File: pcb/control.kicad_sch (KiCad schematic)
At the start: 3 parts, among them J11 Conn_01x02_Pin

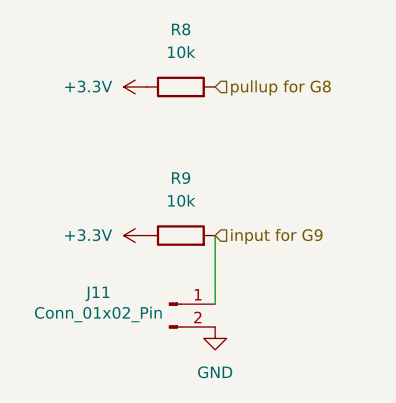
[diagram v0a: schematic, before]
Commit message: Finishing the carrier board with the new usb-c modul
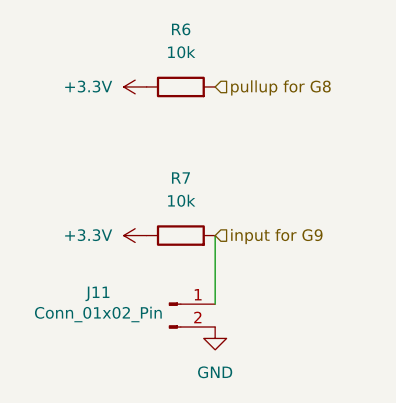
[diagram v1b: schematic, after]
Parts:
- renumbered R8 to R6, R9 to R7
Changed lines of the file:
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@@
 		(dnp no)
 		(fields_autoplaced yes)
-		(property "Reference" "#PWR033"
+		(property "Reference" "#PWR031"
 			(at 124.46 111.76 0)
 			(hide yes)
@@
 			(project "pcb"
 				(path "/2955ee96-3683-4cf6-bfa3-83b5e4980920/6ba59ddd-18a4-4e0c-ad10-73ba465496e1"
-					(reference "#PWR033")
+					(reference "#PWR031")
 					(unit 1)
 				)
@@
 		(dnp no)
 		(fields_autoplaced yes)
-		(property "Reference" "R8"
+		(property "Reference" "R6"
 			(at 120.65 72.39 90)
 			(show_name no)
@@
 			(project "pcb"
 				(path "/2955ee96-3683-4cf6-bfa3-83b5e4980920/6ba59ddd-18a4-4e0c-ad10-73ba465496e1"
-					(reference "R8")
+					(reference "R6")
 					(unit 1)
 				)
@@
 		(dnp no)
 		(fields_autoplaced yes)
-		(property "Reference" "#PWR032"
+		(property "Reference" "#PWR030"
 			(at 120.65 95.25 0)
 			(hide yes)
@@
 			(project "pcb"
 				(path "/2955ee96-3683-4cf6-bfa3-83b5e4980920/6ba59ddd-18a4-4e0c-ad10-73ba465496e1"
-					(reference "#PWR032")
+					(reference "#PWR030")
 					(unit 1)
 				)
@@
 		(dnp no)
 		(fields_autoplaced yes)
-		(property "Reference" "#PWR031"
+		(property "Reference" "#PWR029"
 			(at 120.65 78.74 0)
 			(hide yes)
@@
 			(project "pcb"
 				(path "/2955ee96-3683-4cf6-bfa3-83b5e4980920/6ba59ddd-18a4-4e0c-ad10-73ba465496e1"
-					(reference "#PWR031")
+					(reference "#PWR029")
 					(unit 1)
 				)
@@
 		(dnp no)
 		(fields_autoplaced yes)
-		(property "Reference" "R9"
+		(property "Reference" "R7"
 			(at 120.65 88.9 90)
 			(show_name no)
@@
 			(project "pcb"
 				(path "/2955ee96-3683-4cf6-bfa3-83b5e4980920/6ba59ddd-18a4-4e0c-ad10-73ba465496e1"
-					(reference "R9")
+					(reference "R7")
 					(unit 1)
 				)
